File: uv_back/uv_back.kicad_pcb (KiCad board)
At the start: 2 copper layers, 173.9 x 74.8 mm, 29 parts, among them J1 B3B-PH-SM4-TBT(LF)(SN), J2 B3B-PH-SM4-TBT(LF)(SN), J3 B3B-PH-SM4-TBT(LF)(SN), J4 B3B-PH-SM4-TBT(LF)(SN), J5 B3B-PH-SM4-TBT(LF)(SN)_ALT, J6 B3B-PH-SM4-TBT(LF)(SN)_ALT, J7 B3B-PH-SM4-TBT(LF)(SN), J8 B3B-PH-SM4-TBT(LF)(SN), SW1 CHS01TA, SW2 CHS01TA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

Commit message: commit before nightly branch
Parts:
- removed R3, R4: 0, Resistor_SMD:R_0805_2012Metric_Pad1.20x1.40mm_HandSolder
- added J9: B3B-PH-SM4-TBT(LF)(SN)_ALT, eConnector_JST:B3B-PH-SM4, B.Cu at (148.8, 118.8)
- moved J7 79.6 mm to (207.0, 116.5), turned to 180 degrees
- moved J8 70.8 mm to (194.0, 116.5), turned to 180 degrees
- moved J4 53.8 mm to (123.8, 118.8), turned to 180 degrees
- moved SW1 39.6 mm to (110.5, 111.2), turned to 90 degrees
- moved J1 38.3 mm to (111.2, 118.8)
- moved C1 37.2 mm to (79.0, 99.5), turned to 0 degrees
- moved U1 27.3 mm to (86.0, 101.5), turned to 180 degrees
- moved J6 24.5 mm to (136.2, 118.8)
- moved R7 21.5 mm to (138.2, 113.5), turned to -90 degrees
- moved R8 21.3 mm to (134.2, 113.5), turned to -90 degrees
- moved J3 17.2 mm to (86.2, 118.8), turned to 180 degrees
- moved J2 13.4 mm to (73.8, 118.8)
- moved J5 12.7 mm to (98.8, 118.8)
- moved SW2 12.4 mm to (73.2, 111.8), turned to 90 degrees
- moved R10 12.1 mm to (98.3, 94.0), turned to 0 degrees
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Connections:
- J5 pad 2: Net-(C3-Pad1) -> Net-(J5-Pad2)
- J6 pad 2: Net-(C3-Pad1) -> Net-(J6-Pad2)
- R5 pad 1: Net-(R3-Pad2) -> Net-(R5-Pad1)
- R6 pad 1: Net-(R3-Pad2) -> Net-(R5-Pad1)
- R7 pad 1: Net-(R4-Pad2) -> Net-(R7-Pad1)
- R8 pad 1: Net-(R4-Pad2) -> Net-(R7-Pad1)
- U1 pad 1: Net-(R3-Pad1) -> Net-(R5-Pad1)
- U1 pad 2: Net-(R3-Pad1) -> Net-(R5-Pad1)
- U1 pad 6: Net-(R4-Pad1) -> Net-(R7-Pad1)
- U1 pad 7: Net-(R4-Pad1) -> Net-(R7-Pad1)
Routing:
- net +9V: track 0.00 -> 199.8 mm, vias 0 -> 4
- net /SIG_OUT: track 0.00 -> 150.0 mm
- net /VMID: track 0.00 -> 112.5 mm, vias 0 -> 3
- net Net-(R7-Pad1): track 0.00 -> 96.4 mm
- net Net-(J4-Pad2): track 0.00 -> 79.1 mm
- net Net-(J5-Pad2): track 0.00 -> 64.9 mm, vias 0 -> 2
- net Net-(C3-Pad1): track 0.00 -> 58.8 mm
- net GND: track 0.00 -> 33.1 mm, vias 0 -> 10
- net /BATT-: track 0.00 -> 22.4 mm
- net Net-(R5-Pad1): track 0.00 -> 21.8 mm
- net Net-(J3-Pad2): track 0.00 -> 20.6 mm
- net Net-(J2-Pad1): track 0.00 -> 19.8 mm
- net Net-(J1-Pad1): track 0.00 -> 19.6 mm
- net Net-(J6-Pad2): track 0.00 -> 17.6 mm
- net Net-(C3-Pad2): track 0.00 -> 11.3 mm
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- added copper zone on B.Cu, net GND
- added copper zone on In1.Cu, net GND
- added copper zone on In2.Cu, net GND
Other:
- outline, holes or cut-outs redrawn
- copper layers 2 -> 4
- board text added: "+"
- board text added: "-"
- board text added: "BATTERY"
- board text added: "PU"
- board text added: "R"
- board text added: "S"
- board text added: "SE"
- board text added: "SW"
- board text added: "T"
- board text added: "TRS JACK"
- board text removed: "PICKUP"
- board text removed: "SWITCH"

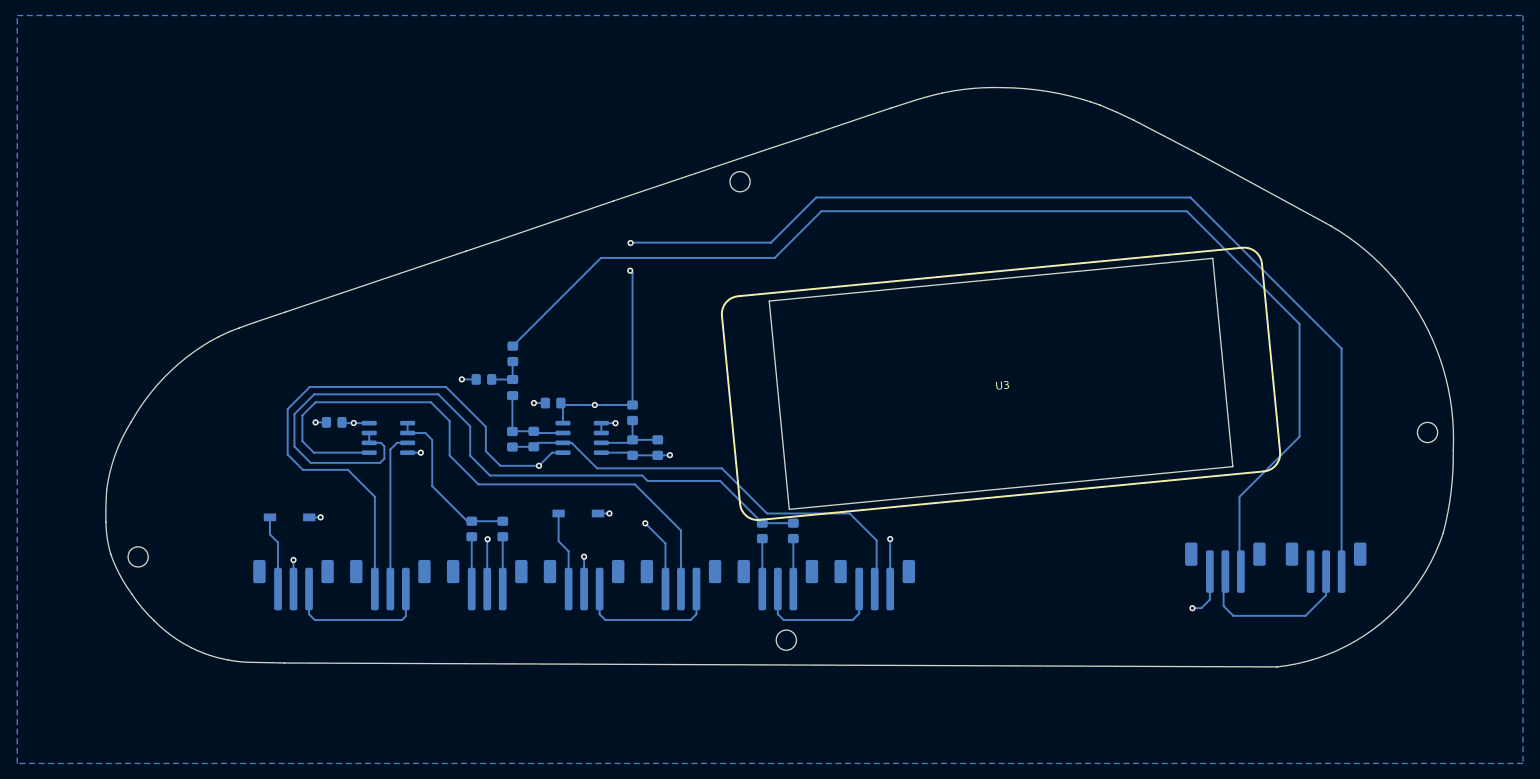
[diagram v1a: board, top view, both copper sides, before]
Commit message: logos in place
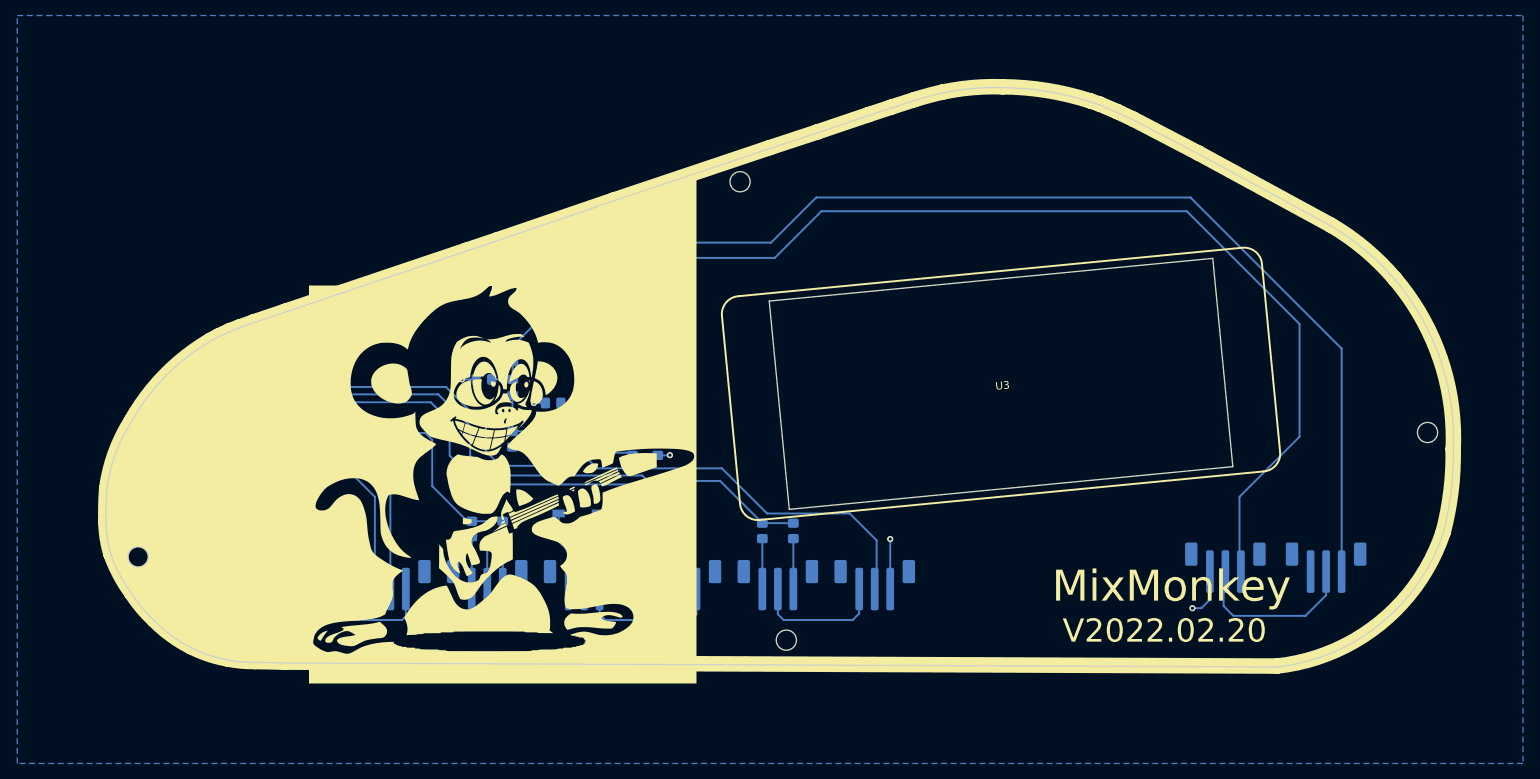
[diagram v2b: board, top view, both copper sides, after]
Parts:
- added G***: LOGO, eLogo:MonkeyGuitar35, F.Cu at (100.8, 107.5)
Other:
- board text added: "MixMonkey"
- board text added: "V2022.02.20"

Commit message: switched to two layer for outline prototype
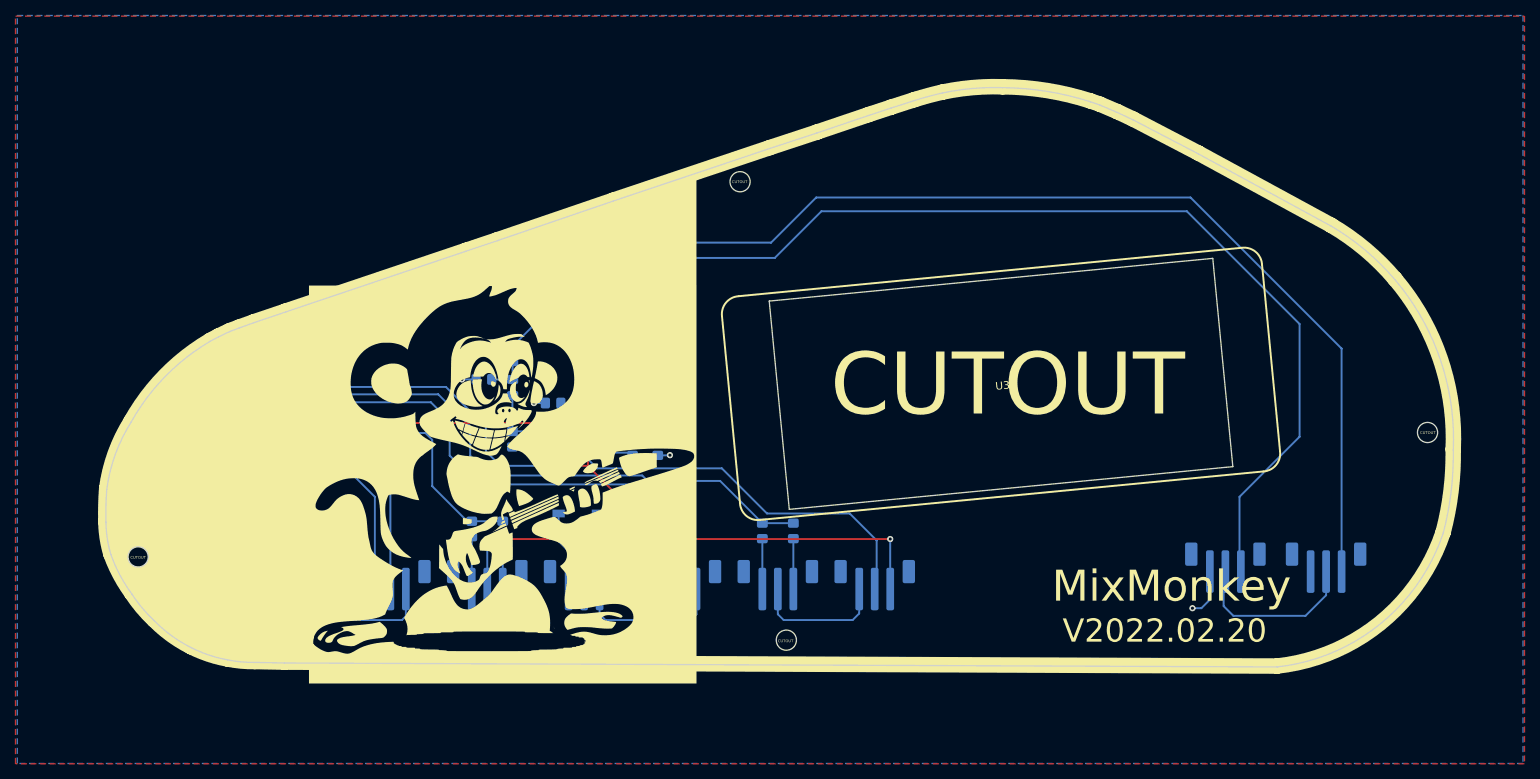
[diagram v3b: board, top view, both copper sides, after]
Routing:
- net /VMID: track 112.5 -> 111.2 mm
- added copper zone on F.Cu, net GND
- removed copper zone on In1.Cu, net GND
- removed copper zone on In2.Cu, net GND
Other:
- copper layers 4 -> 2
- board text added: "CUTOUT"
